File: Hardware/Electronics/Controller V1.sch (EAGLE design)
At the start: 18 parts, among them IC1 SN74AHCT125N, J1 POWER_JACK, J2 0039281023

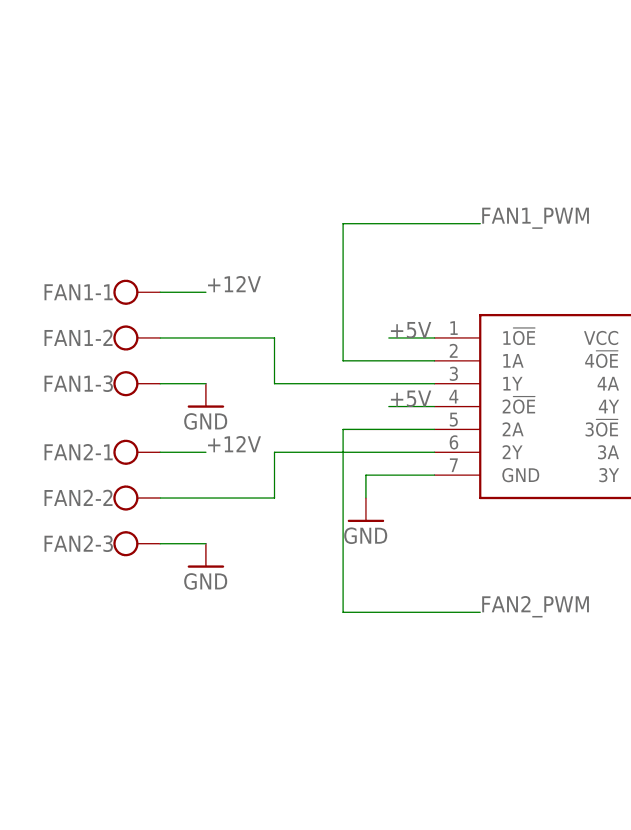
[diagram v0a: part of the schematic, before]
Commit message: Changed screw terminals for actual 4 pin PWM fan headers
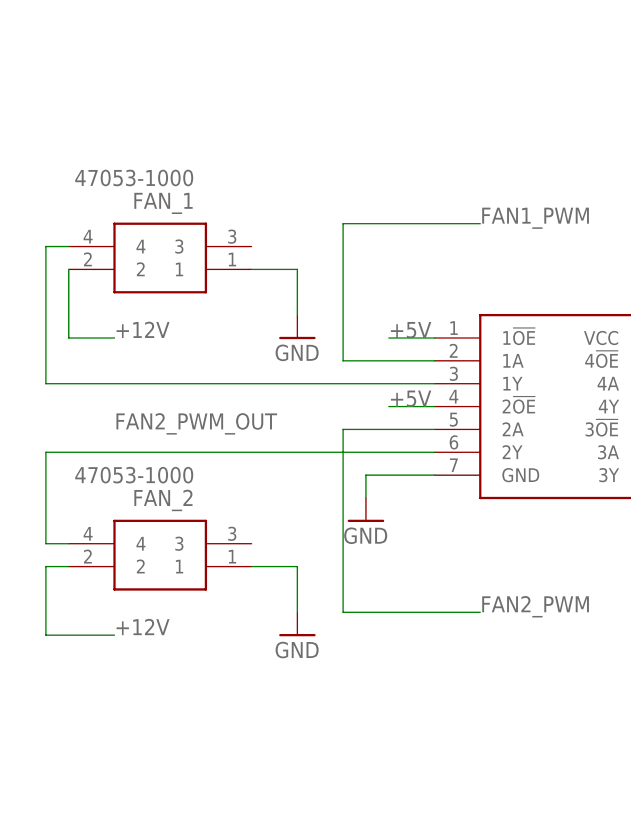
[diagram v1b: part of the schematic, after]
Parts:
- removed FAN1, FAN2: (no value), con-wago-500:W237-103
- added FAN_1, FAN_2: 47053-1000, SamacSys_Parts:47053-1000
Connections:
- removed net FAN1_PWM_OUT: FAN1-2.KL, IC1.1Y
- new net FAN!_PWM_OUT: FAN_1.4, IC1.1Y
- net +12V: now also FAN_1.2, FAN_2.2; no longer FAN1-1.KL, FAN2-1.KL
- net FAN2_PWM_OUT: now also FAN_2.4; no longer FAN2-2.KL
- net GND: now also FAN_1.1, FAN_2.1; no longer FAN1-3.KL, FAN2-3.KL
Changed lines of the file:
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@@
 <part name="J1" library="SparkFun-Connectors" deviceset="POWER_JACK" device=""/>
 <part name="GND11" library="supply1" library_urn="urn:adsk.eagle:library:371" deviceset="GND" device=""/>
-<part name="FAN1" library="con-wago-500" library_urn="urn:adsk.eagle:library:195" deviceset="W237-103" device="" package3d_urn="urn:adsk.eagle:package:10691/1"/>
-<part name="FAN2" library="con-wago-500" library_urn="urn:adsk.eagle:library:195" deviceset="W237-103" device="" package3d_urn="urn:adsk.eagle:package:10691/1"/>
-<part name="GND8" library="supply1" library_urn="urn:adsk.eagle:library:371" deviceset="GND" device=""/>
-<part name="GND9" library="supply1" library_urn="urn:adsk.eagle:library:371" deviceset="GND" device=""/>
 <part name="GND12" library="supply1" library_urn="urn:adsk.eagle:library:371" deviceset="GND" device=""/>
 <part name="GND13" library="supply1" library_urn="urn:adsk.eagle:library:371" deviceset="GND" device=""/>
@@
 <part name="GPIO" library="SparkFun-Connectors" deviceset="CONN_06" device="SILK_FEMALE_PTH"/>
 <part name="GND23" library="supply1" library_urn="urn:adsk.eagle:library:371" deviceset="GND" device=""/>
+<part name="FAN_1" library="SamacSys_Parts" deviceset="47053-1000" device=""/>
+<part name="FAN_2" library="SamacSys_Parts" deviceset="47053-1000" device=""/>
+<part name="GND8" library="supply1" library_urn="urn:adsk.eagle:library:371" deviceset="GND" device=""/>
+<part name="GND9" library="supply1" library_urn="urn:adsk.eagle:library:371" deviceset="GND" device=""/>
 </parts>
 <sheets>
@@
 <attribute name="VALUE" x="-81.28" y="142.24" size="1.778" layer="96"/>
 </instance>
-<instance part="FAN1" gate="-1" x="-101.6" y="55.88" smashed="yes">
-<attribute name="NAME" x="-101.6" y="56.769" size="1.778" layer="95" rot="R180"/>
-</instance>
-<instance part="FAN1" gate="-2" x="-101.6" y="50.8" smashed="yes">
-<attribute name="NAME" x="-101.6" y="51.689" size="1.778" layer="95" rot="R180"/>
-</instance>
-<instance part="FAN1" gate="-3" x="-101.6" y="45.72" smashed="yes">
-<attribute name="VALUE" x="-104.14" y="42.037" size="1.778" layer="96"/>
-<attribute name="NAME" x="-101.6" y="46.609" size="1.778" layer="95" rot="R180"/>
-</instance>
-<instance part="FAN2" gate="-1" x="-101.6" y="38.1" smashed="yes">
-<attribute name="NAME" x="-101.6" y="38.989" size="1.778" layer="95" rot="R180"/>
-</instance>
-<instance part="FAN2" gate="-2" x="-101.6" y="33.02" smashed="yes">
-<attribute name="NAME" x="-101.6" y="33.909" size="1.778" layer="95" rot="R180"/>
-</instance>
-<instance part="FAN2" gate="-3" x="-101.6" y="27.94" smashed="yes">
-<attribute name="VALUE" x="-104.14" y="24.257" size="1.778" layer="96"/>
-<attribute name="NAME" x="-101.6" y="28.829" size="1.778" layer="95" rot="R180"/>
-</instance>
-<instance part="GND8" gate="1" x="-91.44" y="25.4" smashed="yes">
-<attribute name="VALUE" x="-93.98" y="22.86" size="1.778" layer="96"/>
-</instance>
-<instance part="GND9" gate="1" x="-91.44" y="43.18" smashed="yes">
-<attribute name="VALUE" x="-93.98" y="40.64" size="1.778" layer="96"/>
-</instance>
 <instance part="GND12" gate="1" x="48.26" y="43.18" smashed="yes">
 <attribute name="VALUE" x="45.72" y="40.64" size="1.778" layer="96"/>
@@
 <instance part="GND23" gate="1" x="48.26" y="17.78" smashed="yes">
 <attribute name="VALUE" x="45.72" y="15.24" size="1.778" layer="96"/>
+</instance>
+<instance part="FAN_1" gate="G$1" x="-86.36" y="58.42" smashed="yes" rot="R180">
+<attribute name="NAME" x="-92.71" y="66.04" size="1.778" layer="95" rot="R180" align="center-left"/>
+<attribute name="VALUE" x="-92.71" y="68.58" size="1.778" layer="96" rot="R180" align="center-left"/>
+</instance>
+<instance part="FAN_2" gate="G$1" x="-86.36" y="25.4" smashed="yes" rot="R180">
+<attribute name="NAME" x="-92.71" y="33.02" size="1.778" layer="95" rot="R180" align="center-left"/>
+<attribute name="VALUE" x="-92.71" y="35.56" size="1.778" layer="96" rot="R180" align="center-left"/>
+</instance>
+<instance part="GND8" gate="1" x="-81.28" y="50.8" smashed="yes">
+<attribute name="VALUE" x="-83.82" y="48.26" size="1.778" layer="96"/>
+</instance>
+<instance part="GND9" gate="1" x="-81.28" y="17.78" smashed="yes">
+<attribute name="VALUE" x="-83.82" y="15.24" size="1.778" layer="96"/>
 </instance>
 </instances>
@@
 <wire x1="-78.74" y1="152.4" x2="-78.74" y2="147.32" width="0.1524" layer="91"/>
 <pinref part="GND11" gate="1" pin="GND"/>
-</segment>
-<segment>
-<pinref part="FAN2" gate="-3" pin="KL"/>
-<wire x1="-96.52" y1="27.94" x2="-91.44" y2="27.94" width="0.1524" layer="91"/>
-<pinref part="GND8" gate="1" pin="GND"/>
-</segment>
-<segment>
-<pinref part="FAN1" gate="-3" pin="KL"/>
-<wire x1="-96.52" y1="45.72" x2="-91.44" y2="45.72" width="0.1524" layer="91"/>
-<pinref part="GND9" gate="1" pin="GND"/>
 </segment>
 <segment>
@@
 <wire x1="48.26" y1="25.4" x2="48.26" y2="20.32" width="0.1524" layer="91"/>
 <pinref part="GND23" gate="1" pin="GND"/>
+</segment>
+<segment>
+<pinref part="FAN_1" gate="G$1" pin="1"/>
+<wire x1="-86.36" y1="58.42" x2="-81.28" y2="58.42" width="0.1524" layer="91"/>
+<wire x1="-81.28" y1="58.42" x2="-81.28" y2="53.34" width="0.1524" layer="91"/>
+<pinref part="GND8" gate="1" pin="GND"/>
+</segment>
+<segment>
+<pinref part="FAN_2" gate="G$1" pin="1"/>
+<wire x1="-86.36" y1="25.4" x2="-81.28" y2="25.4" width="0.1524" layer="91"/>
+<wire x1="-81.28" y1="25.4" x2="-81.28" y2="20.32" width="0.1524" layer="91"/>
+<pinref part="GND9" gate="1" pin="GND"/>
 </segment>
 </net>
@@
 </segment>
 </net>
-<net name="FAN1_PWM_OUT" class="0">
-<segment>
-<pinref part="IC1" gate="G$1" pin="1Y"/>
-<wire x1="-66.04" y1="45.72" x2="-83.82" y2="45.72" width="0.1524" layer="91"/>
-<wire x1="-83.82" y1="45.72" x2="-83.82" y2="50.8" width="0.1524" layer="91"/>
-<pinref part="FAN1" gate="-2" pin="KL"/>
-<wire x1="-96.52" y1="50.8" x2="-83.82" y2="50.8" width="0.1524" layer="91"/>
-</segment>
-</net>
 <net name="+12V" class="0">
 <segment>
@@
 </segment>
 <segment>
-<pinref part="FAN1" gate="-1" pin="KL"/>
-<wire x1="-96.52" y1="55.88" x2="-91.44" y2="55.88" width="0.1524" layer="91"/>
-<label x="-91.44" y="55.88" size="1.778" layer="95"/>
-</segment>
-<segment>
-<pinref part="FAN2" gate="-1" pin="KL"/>
-<wire x1="-96.52" y1="38.1" x2="-91.44" y2="38.1" width="0.1524" layer="91"/>
-<label x="-91.44" y="38.1" size="1.778" layer="95"/>
-</segment>
-</net>
-<net name="FAN2_PWM_OUT" class="0">
-<segment>
-<pinref part="IC1" gate="G$1" pin="2Y"/>
-<wire x1="-66.04" y1="38.1" x2="-83.82" y2="38.1" width="0.1524" layer="91"/>
-<wire x1="-83.82" y1="38.1" x2="-83.82" y2="33.02" width="0.1524" layer="91"/>
-<pinref part="FAN2" gate="-2" pin="KL"/>
-<wire x1="-83.82" y1="33.02" x2="-96.52" y2="33.02" width="0.1524" layer="91"/>
+<pinref part="FAN_1" gate="G$1" pin="2"/>
+<wire x1="-106.68" y1="58.42" x2="-106.68" y2="50.8" width="0.1524" layer="91"/>
+<wire x1="-106.68" y1="50.8" x2="-101.6" y2="50.8" width="0.1524" layer="91"/>
+<label x="-101.6" y="50.8" size="1.778" layer="95"/>
+</segment>
+<segment>
+<pinref part="FAN_2" gate="G$1" pin="2"/>
+<wire x1="-106.68" y1="25.4" x2="-109.22" y2="25.4" width="0.1524" layer="91"/>
+<wire x1="-109.22" y1="25.4" x2="-109.22" y2="17.78" width="0.1524" layer="91"/>
+<wire x1="-109.22" y1="17.78" x2="-101.6" y2="17.78" width="0.1524" layer="91"/>
+<label x="-101.6" y="17.78" size="1.778" layer="95"/>
 </segment>
 </net>
@@
 </segment>
 </net>
+<net name="FAN2_PWM_OUT" class="0">
+<segment>
+<pinref part="IC1" gate="G$1" pin="2Y"/>
+<wire x1="-66.04" y1="38.1" x2="-109.22" y2="38.1" width="0.1524" layer="91"/>
+<wire x1="-109.22" y1="38.1" x2="-109.22" y2="27.94" width="0.1524" layer="91"/>
+<pinref part="FAN_2" gate="G$1" pin="4"/>
+<wire x1="-109.22" y1="27.94" x2="-106.68" y2="27.94" width="0.1524" layer="91"/>
+<label x="-101.6" y="40.64" size="1.778" layer="95"/>
+</segment>
+</net>
+<net name="FAN!_PWM_OUT" class="0">
+<segment>
+<pinref part="FAN_1" gate="G$1" pin="4"/>
+<wire x1="-109.22" y1="45.72" x2="-109.22" y2="60.96" width="0.1524" layer="91"/>
+<wire x1="-109.22" y1="60.96" x2="-106.68" y2="60.96" width="0.1524" layer="91"/>
+<pinref part="IC1" gate="G$1" pin="1Y"/>
+<wire x1="-66.04" y1="45.72" x2="-109.22" y2="45.72" width="0.1524" layer="91"/>
+</segment>
+</net>
